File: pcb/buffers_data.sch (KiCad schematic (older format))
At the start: 8 parts, among them U1 74LVCH162245A, U2 74LVCH162245A

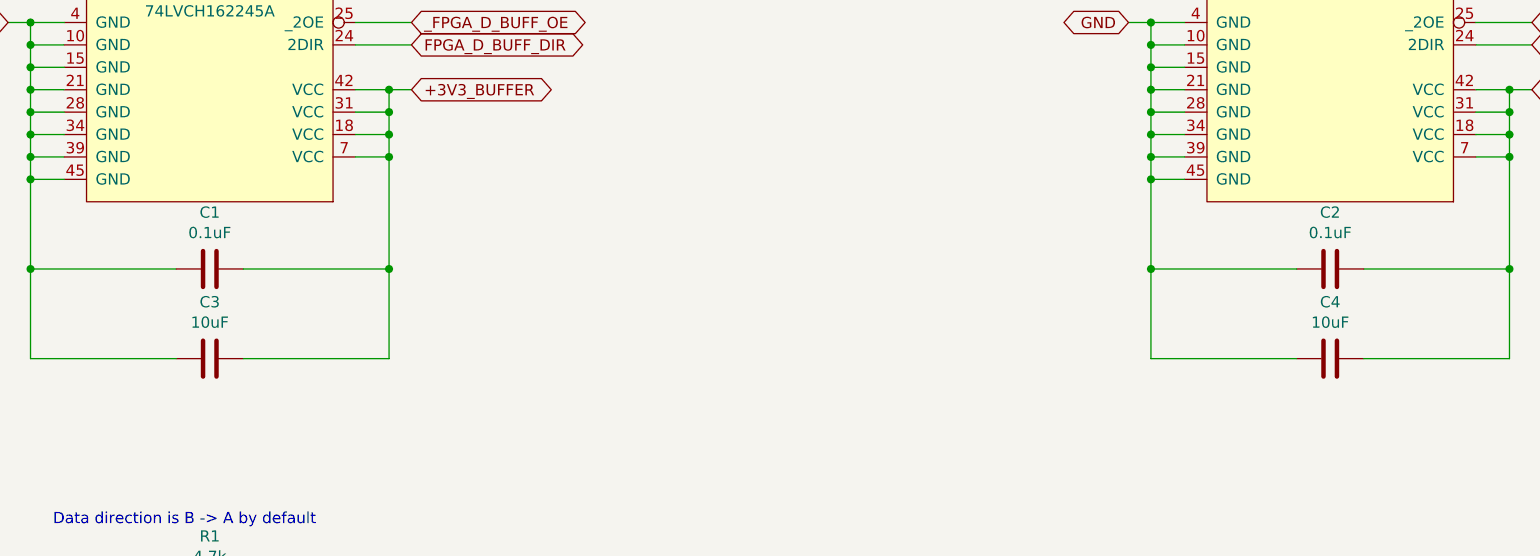
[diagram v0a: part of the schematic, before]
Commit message: more footprints assigned, caps added into open collector base circuit
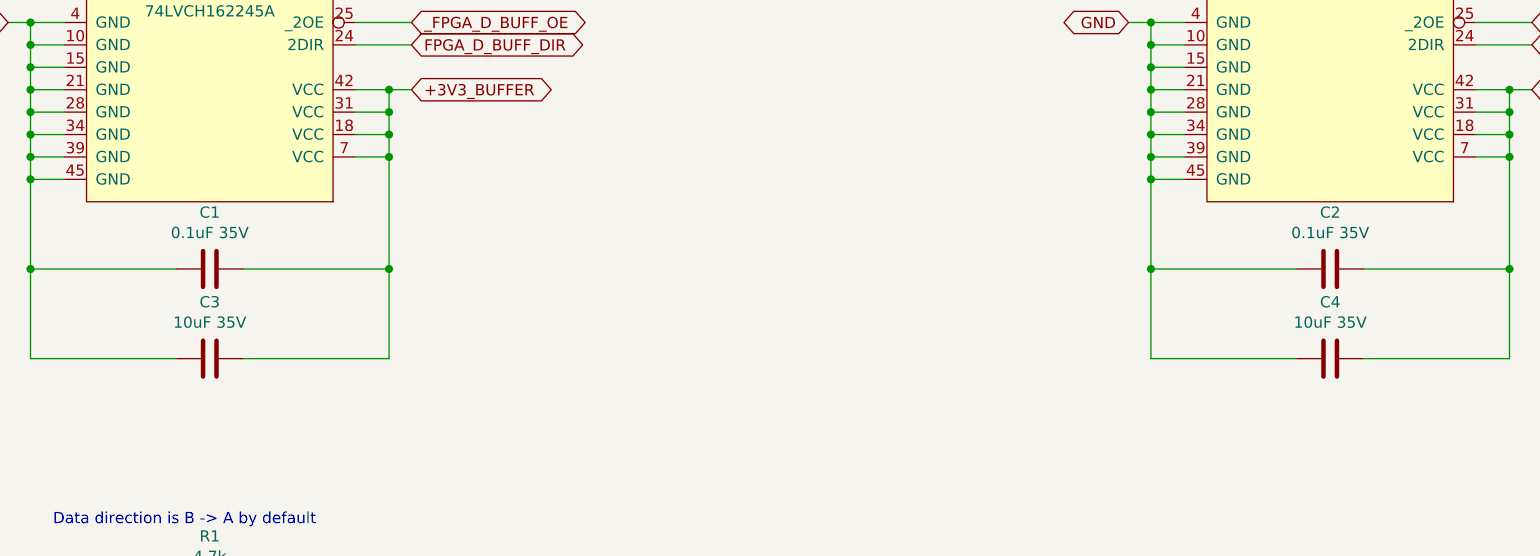
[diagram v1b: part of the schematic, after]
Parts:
- C1, C2: value 0.1uF -> 0.1uF 35V; footprint (none) -> Capacitor_SMD:C_0603_1608Metric_Pad1.05x0.95mm_HandSolder
- C3, C4: value 10uF -> 10uF 35V; footprint (none) -> Capacitor_SMD:C_1210_3225Metric_Pad1.42x2.65mm_HandSolder
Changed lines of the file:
@@
 P 3250 5600
 F 0 "C3" V 3502 5600 50  0000 C CNN
-F 1 "10uF" V 3411 5600 50  0000 C CNN
-F 2 "" H 3288 5450 50  0001 C CNN
+F 1 "10uF 35V" V 3411 5600 50  0000 C CNN
+F 2 "Capacitor_SMD:C_1210_3225Metric_Pad1.42x2.65mm_HandSolder" H 3288 5450 50  0001 C CNN
 F 3 "~" H 3250 5600 50  0001 C CNN
 	1    3250 5600
@@
 P 3250 5200
 F 0 "C1" V 3502 5200 50  0000 C CNN
-F 1 "0.1uF" V 3411 5200 50  0000 C CNN
-F 2 "" H 3288 5050 50  0001 C CNN
+F 1 "0.1uF 35V" V 3411 5200 50  0000 C CNN
+F 2 "Capacitor_SMD:C_0603_1608Metric_Pad1.05x0.95mm_HandSolder" H 3288 5050 50  0001 C CNN
 F 3 "~" H 3250 5200 50  0001 C CNN
 	1    3250 5200
@@
 P 8250 5600
 F 0 "C4" V 8502 5600 50  0000 C CNN
-F 1 "10uF" V 8411 5600 50  0000 C CNN
-F 2 "" H 8288 5450 50  0001 C CNN
+F 1 "10uF 35V" V 8411 5600 50  0000 C CNN
+F 2 "Capacitor_SMD:C_1210_3225Metric_Pad1.42x2.65mm_HandSolder" H 8288 5450 50  0001 C CNN
 F 3 "~" H 8250 5600 50  0001 C CNN
 	1    8250 5600
@@
 P 8250 5200
 F 0 "C2" V 8502 5200 50  0000 C CNN
-F 1 "0.1uF" V 8411 5200 50  0000 C CNN
-F 2 "" H 8288 5050 50  0001 C CNN
+F 1 "0.1uF 35V" V 8411 5200 50  0000 C CNN
+F 2 "Capacitor_SMD:C_0603_1608Metric_Pad1.05x0.95mm_HandSolder" H 8288 5050 50  0001 C CNN
 F 3 "~" H 8250 5200 50  0001 C CNN
 	1    8250 5200

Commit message: working on pcb 2
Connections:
- net D0 is gone; now on net D8: U2.23 (2B7)
- net D1 is gone; now on net D9: U2.22 (2B6)
- net D2 is gone; now on net D10: U2.20 (2B5)
- net D3 is gone; now on net D11: U2.19 (2B4)
- net D4 is gone; now on net D12: U2.17 (2B3)
- net D5 is gone; now on net D13: U2.16 (2B2)
- net D6 is gone; now on net D14: U2.14 (2B1)
- net D7 is gone; now on net D15: U2.13 (2B0)
- net FPGA_D0 is gone; now on net FPGA_D8: U2.26 (2A7)
- net FPGA_D1 is gone; now on net FPGA_D9: U2.27 (2A6)
- net FPGA_D2 is gone; now on net FPGA_D10: U2.29 (2A5)
- net FPGA_D3 is gone; now on net FPGA_D11: U2.30 (2A4)
- net FPGA_D4 is gone; now on net FPGA_D12: U2.32 (2A3)
- net FPGA_D5 is gone; now on net FPGA_D13: U2.33 (2A2)
- net FPGA_D6 is gone; now on net FPGA_D14: U2.35 (2A1)
- net FPGA_D7 is gone; now on net FPGA_D15: U2.36 (2A0)
- net D10: no longer U2.9 (1B5)
- net D11: no longer U2.8 (1B4)
- net D12: no longer U2.6 (1B3)
- net D13: no longer U2.5 (1B2)
- net D14: no longer U2.3 (1B1)
- net D15: no longer U2.2 (1B0)
- net D16: now also U2.12 (1B7); no longer U1.23 (2B7)
- net D17: now also U2.11 (1B6); no longer U1.22 (2B6)
- net D18: now also U2.9 (1B5); no longer U1.20 (2B5)
- net D19: now also U2.8 (1B4); no longer U1.19 (2B4)
- net D20: now also U2.6 (1B3); no longer U1.17 (2B3)
- net D21: now also U2.5 (1B2); no longer U1.16 (2B2)
- net D22: now also U2.3 (1B1); no longer U1.14 (2B1)
- net D23: now also U2.2 (1B0); no longer U1.13 (2B0)
- net D24: now also U1.23 (2B7); no longer U1.12 (1B7)
- net D25: now also U1.22 (2B6); no longer U1.11 (1B6)
- net D26: now also U1.20 (2B5); no longer U1.9 (1B5)
- net D27: now also U1.19 (2B4); no longer U1.8 (1B4)
- net D28: now also U1.17 (2B3); no longer U1.6 (1B3)
- net D29: now also U1.16 (2B2); no longer U1.5 (1B2)
- net D30: now also U1.14 (2B1); no longer U1.3 (1B1)
- net D31: now also U1.13 (2B0); no longer U1.2 (1B0)
- net D8: no longer U2.12 (1B7)
- net D9: no longer U2.11 (1B6)
- net FPGA_D10: no longer U2.40 (1A5)
- net FPGA_D11: no longer U2.41 (1A4)
- net FPGA_D12: no longer U2.43 (1A3)
- net FPGA_D13: no longer U2.44 (1A2)
- net FPGA_D14: no longer U2.46 (1A1)
- net FPGA_D15: no longer U2.47 (1A0)
- net FPGA_D16: now also U2.37 (1A7); no longer U1.26 (2A7)
- net FPGA_D17: now also U2.38 (1A6); no longer U1.27 (2A6)
- net FPGA_D18: now also U2.40 (1A5); no longer U1.29 (2A5)
- net FPGA_D19: now also U2.41 (1A4); no longer U1.30 (2A4)
- net FPGA_D20: now also U2.43 (1A3); no longer U1.32 (2A3)
- net FPGA_D21: now also U2.44 (1A2); no longer U1.33 (2A2)
- net FPGA_D22: now also U2.46 (1A1); no longer U1.35 (2A1)
- net FPGA_D23: now also U2.47 (1A0); no longer U1.36 (2A0)
- net FPGA_D24: now also U1.26 (2A7); no longer U1.37 (1A7)
- net FPGA_D25: now also U1.27 (2A6); no longer U1.38 (1A6)
- net FPGA_D26: now also U1.29 (2A5); no longer U1.40 (1A5)
- net FPGA_D27: now also U1.30 (2A4); no longer U1.41 (1A4)
- net FPGA_D28: now also U1.32 (2A3); no longer U1.43 (1A3)
- net FPGA_D29: now also U1.33 (2A2); no longer U1.44 (1A2)
- net FPGA_D30: now also U1.35 (2A1); no longer U1.46 (1A1)
- net FPGA_D31: now also U1.36 (2A0); no longer U1.47 (1A0)
- net FPGA_D8: no longer U2.37 (1A7)
- net FPGA_D9: no longer U2.38 (1A6)
- net FPGA_D_BUFF_DIR: no longer U1.1 (1DIR)
- net _FPGA_D_BUFF_OE: no longer U1.48 (_1OE)
- new net A0: U1.12 (1B7)
- new net A1: U1.11 (1B6)
- new net A2: U1.9 (1B5)
- new net A3: U1.8 (1B4)
- new net A4: U1.6 (1B3)
- new net A5: U1.5 (1B2)
- new net A6: U1.3 (1B1)
- new net A7: U1.2 (1B0)
- new net FPGA_A0: U1.47 (1A0)
- new net FPGA_A1: U1.46 (1A1)
- new net FPGA_A2: U1.44 (1A2)
- new net FPGA_A3: U1.43 (1A3)
- new net FPGA_A4: U1.41 (1A4)
- new net FPGA_A5: U1.40 (1A5)
- new net FPGA_A6: U1.38 (1A6)
- new net FPGA_A7: U1.37 (1A7)
- new net FPGA_A_BUFF_DIR: U1.1 (1DIR)
- new net _FPGA_A_BUFF_OE: U1.48 (_1OE)

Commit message: Board pcb updated
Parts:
- C3, C4: value 10uF 35V -> 1uF 35V; footprint Capacitor_SMD:C_1210_3225Metric_Pad1.42x2.65mm_HandSolder -> Capacitor_SMD:C_0805_2012Metric_Pad1.15x1.40mm_HandSolder
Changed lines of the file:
@@
 P 3250 5600
 F 0 "C3" V 3502 5600 50  0000 C CNN
-F 1 "10uF 35V" V 3411 5600 50  0000 C CNN
-F 2 "Capacitor_SMD:C_1210_3225Metric_Pad1.42x2.65mm_HandSolder" H 3288 5450 50  0001 C CNN
+F 1 "1uF 35V" V 3411 5600 50  0000 C CNN
+F 2 "Capacitor_SMD:C_0805_2012Metric_Pad1.15x1.40mm_HandSolder" H 3288 5450 50  0001 C CNN
 F 3 "~" H 3250 5600 50  0001 C CNN
 	1    3250 5600
@@
 P 8250 5600
 F 0 "C4" V 8502 5600 50  0000 C CNN
-F 1 "10uF 35V" V 8411 5600 50  0000 C CNN
-F 2 "Capacitor_SMD:C_1210_3225Metric_Pad1.42x2.65mm_HandSolder" H 8288 5450 50  0001 C CNN
+F 1 "1uF 35V" V 8411 5600 50  0000 C CNN
+F 2 "Capacitor_SMD:C_0805_2012Metric_Pad1.15x1.40mm_HandSolder" H 8288 5450 50  0001 C CNN
 F 3 "~" H 8250 5600 50  0001 C CNN
 	1    8250 5600

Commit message: some more work done
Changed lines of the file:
@@
 Text GLabel 9150 4200 2    50   BiDi ~ 0
 FPGA_D_BUFF_DIR
-Text GLabel 9150 1550 2    50   BiDi ~ 0
+Text GLabel 9200 1550 2    50   BiDi ~ 0
 FPGA_D23
-Text GLabel 9150 1650 2    50   BiDi ~ 0
+Text GLabel 9200 1650 2    50   BiDi ~ 0
 FPGA_D22
-Text GLabel 9150 1750 2    50   BiDi ~ 0
+Text GLabel 9200 1750 2    50   BiDi ~ 0
 FPGA_D21
-Text GLabel 9150 1850 2    50   BiDi ~ 0
+Text GLabel 9200 1850 2    50   BiDi ~ 0
 FPGA_D20
-Text GLabel 9150 1950 2    50   BiDi ~ 0
+Text GLabel 9200 1950 2    50   BiDi ~ 0
 FPGA_D19
-Text GLabel 9150 2050 2    50   BiDi ~ 0
+Text GLabel 9200 2050 2    50   BiDi ~ 0
 FPGA_D18
-Text GLabel 9150 2150 2    50   BiDi ~ 0
+Text GLabel 9200 2150 2    50   BiDi ~ 0
 FPGA_D17
-Text GLabel 9150 2250 2    50   BiDi ~ 0
+Text GLabel 9200 2250 2    50   BiDi ~ 0
 FPGA_D16
-Text GLabel 9150 3200 2    50   BiDi ~ 0
+Text GLabel 9200 3200 2    50   BiDi ~ 0
 FPGA_D15
-Text GLabel 9150 3300 2    50   BiDi ~ 0
+Text GLabel 9200 3300 2    50   BiDi ~ 0
 FPGA_D14
-Text GLabel 9150 3400 2    50   BiDi ~ 0
+Text GLabel 9200 3400 2    50   BiDi ~ 0
 FPGA_D13
-Text GLabel 9150 3500 2    50   BiDi ~ 0
+Text GLabel 9200 3500 2    50   BiDi ~ 0
 FPGA_D12
-Text GLabel 9150 3600 2    50   BiDi ~ 0
+Text GLabel 9200 3600 2    50   BiDi ~ 0
 FPGA_D11
-Text GLabel 9150 3700 2    50   BiDi ~ 0
+Text GLabel 9200 3700 2    50   BiDi ~ 0
 FPGA_D10
-Text GLabel 9150 3800 2    50   BiDi ~ 0
+Text GLabel 9200 3800 2    50   BiDi ~ 0
 FPGA_D9
-Text GLabel 9150 3900 2    50   BiDi ~ 0
+Text GLabel 9200 3900 2    50   BiDi ~ 0
 FPGA_D8
 Wire Wire Line
@@
 Wire Wire Line
 	4150 4100 3900 4100
-Text GLabel 4150 3900 2    50   BiDi ~ 0
+Text GLabel 4200 3900 2    50   BiDi ~ 0
 FPGA_D24
-Text GLabel 4150 3800 2    50   BiDi ~ 0
+Text GLabel 4200 3800 2    50   BiDi ~ 0
 FPGA_D25
-Text GLabel 4150 3700 2    50   BiDi ~ 0
+Text GLabel 4200 3700 2    50   BiDi ~ 0
 FPGA_D26
-Text GLabel 4150 3600 2    50   BiDi ~ 0
+Text GLabel 4200 3600 2    50   BiDi ~ 0
 FPGA_D27
-Text GLabel 4150 3500 2    50   BiDi ~ 0
+Text GLabel 4200 3500 2    50   BiDi ~ 0
 FPGA_D28
-Text GLabel 4150 3400 2    50   BiDi ~ 0
+Text GLabel 4200 3400 2    50   BiDi ~ 0
 FPGA_D29
-Text GLabel 4150 3300 2    50   BiDi ~ 0
+Text GLabel 4200 3300 2    50   BiDi ~ 0
 FPGA_D30
-Text GLabel 4150 3200 2    50   BiDi ~ 0
+Text GLabel 4200 3200 2    50   BiDi ~ 0
 FPGA_D31
 Text GLabel 4150 4200 2    50   BiDi ~ 0
@@
 Wire Wire Line
 	3900 3200 4150 3200
-Text GLabel 4200 1550 2    50   BiDi ~ 0
+Text GLabel 4250 1550 2    50   BiDi ~ 0
 FPGA_A0
-Text GLabel 4200 1650 2    50   BiDi ~ 0
+Text GLabel 4250 1650 2    50   BiDi ~ 0
 FPGA_A1
-Text GLabel 4200 1750 2    50   BiDi ~ 0
+Text GLabel 4250 1750 2    50   BiDi ~ 0
 FPGA_A2
-Text GLabel 4200 1850 2    50   BiDi ~ 0
+Text GLabel 4250 1850 2    50   BiDi ~ 0
 FPGA_A3
-Text GLabel 4200 1950 2    50   BiDi ~ 0
+Text GLabel 4250 1950 2    50   BiDi ~ 0
 FPGA_A4
-Text GLabel 4200 2050 2    50   BiDi ~ 0
+Text GLabel 4250 2050 2    50   BiDi ~ 0
 FPGA_A5
-Text GLabel 4200 2150 2    50   BiDi ~ 0
+Text GLabel 4250 2150 2    50   BiDi ~ 0
 FPGA_A6
-Text GLabel 4200 2250 2    50   BiDi ~ 0
+Text GLabel 4250 2250 2    50   BiDi ~ 0
 FPGA_A7
 Wire Wire Line
